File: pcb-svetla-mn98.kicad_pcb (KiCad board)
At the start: 2 copper layers, 32 x 35.6 mm, 7 parts, among them J1 TURN PAIRS, J14 P6DC INPUT, J2 MAIN LIGHTS, J3 AUX LIGHTS

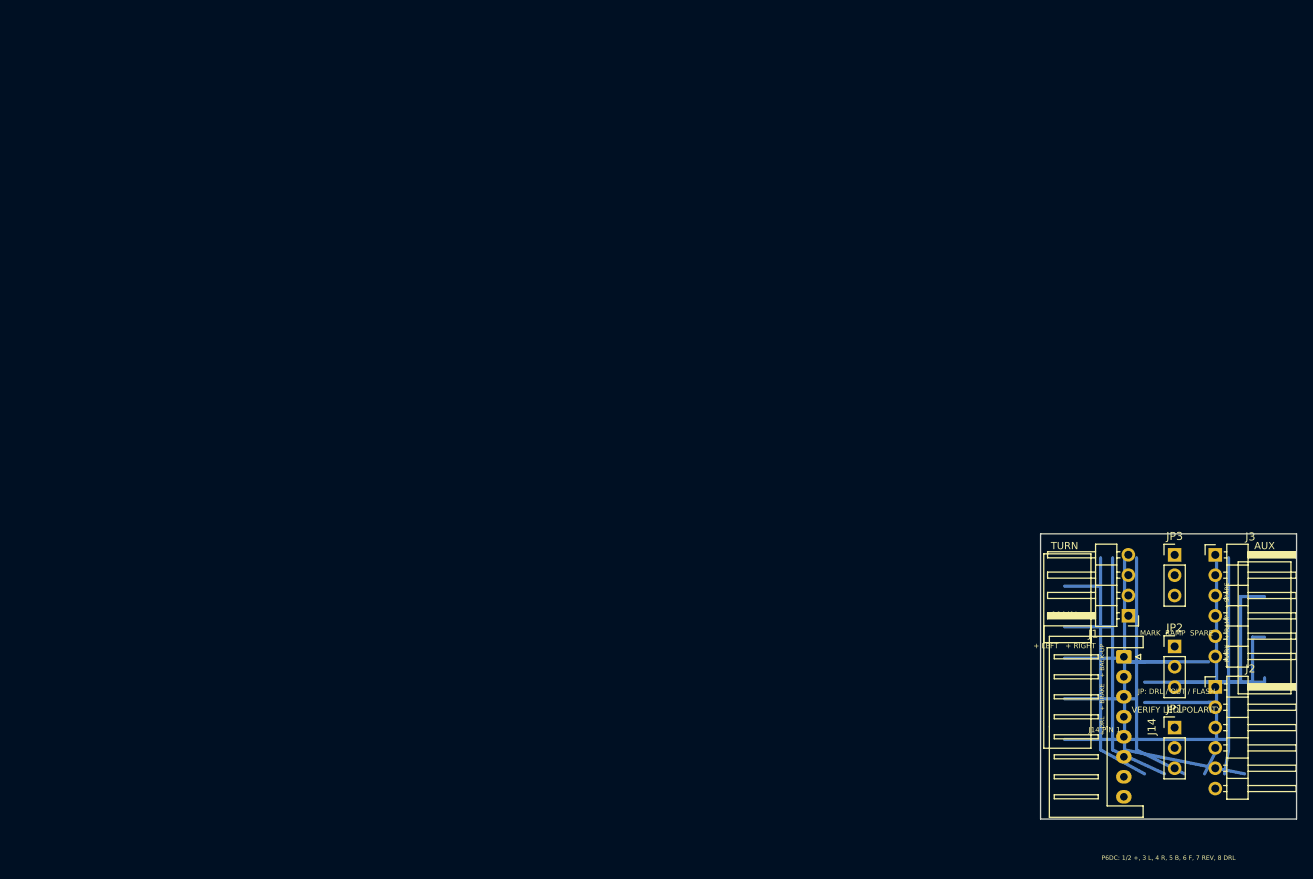
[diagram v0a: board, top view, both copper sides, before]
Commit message: Revise body distributor placement
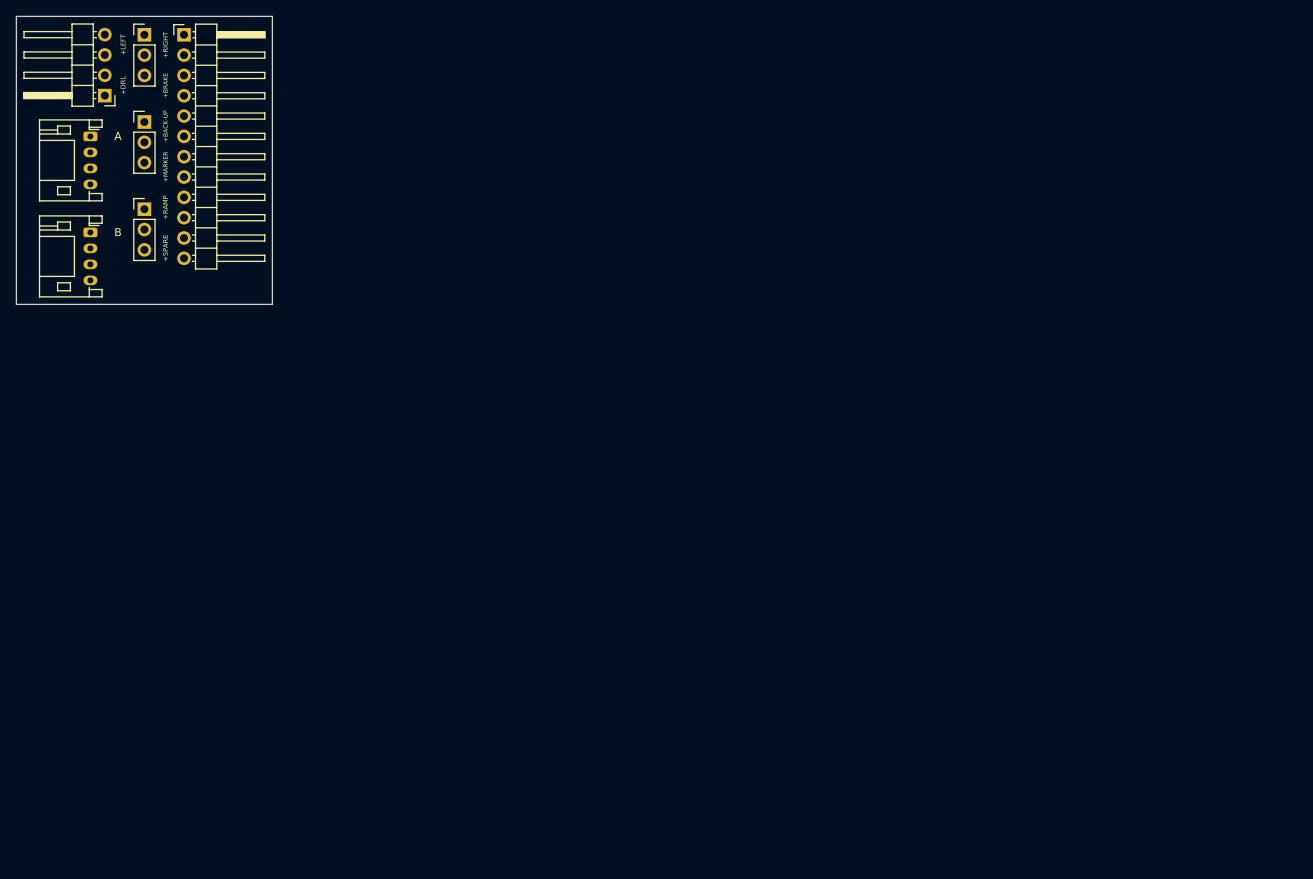
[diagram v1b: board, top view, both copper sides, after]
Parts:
- removed J3: AUX LIGHTS, PinHeader_1x06_P2.54mm_Horizontal
- added J15: BODY LINK B, JST_PH_S4B-PH-K_1x04_P2.00mm_Horizontal, F.Cu at (9.25, 27.0)
- J1: value TURN PAIRS -> LEFT LIGHT PORTS
- J14: value P6DC INPUT -> BODY LINK A; footprint JST_XH_S8B-XH-A_1x08_P2.50mm_Horizontal -> JST_PH_S4B-PH-K_1x04_P2.00mm_Horizontal
- J2: value MAIN LIGHTS -> RIGHT LIGHT PORTS; footprint PinHeader_1x06_P2.54mm_Horizontal -> PinHeader_1x12_P2.54mm_Horizontal
- moved JP1 155.2 mm to (16.0, 2.30)
- moved J2 152.5 mm to (20.9, 2.30)
- moved J14 144.6 mm to (9.25, 15.0)
- moved JP2 144.5 mm to (16.0, 13.2)
- moved J1 143.5 mm to (11.1, 9.90)
- moved JP3 135.8 mm to (16.0, 24.1)
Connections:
- J1 pad 1: RIGHT -> DRL
- J14 pad 2: COMMON+ -> LEFT
- J14 pad 3: LEFT -> RIGHT
- J14 pad 4: RIGHT -> BRAKE
- J2 pad 1: BACK-UP -> COMMON+
- J2 pad 2: COMMON+ -> RIGHT
- J2 pad 3: BRAKE -> COMMON+
- J2 pad 4: COMMON+ -> BRAKE
- J2 pad 5: DRL -> COMMON+
- J2 pad 6: COMMON+ -> BACK-UP
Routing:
- net DRL: track 66.3 -> 0.00 mm
- net BACK-UP: track 47.5 -> 0.00 mm
- net FLASH: track 42.4 -> 0.00 mm
- net BRAKE: track 39.7 -> 0.00 mm
- net RIGHT: track 37.2 -> 0.00 mm
- net LEFT: track 34.8 -> 0.00 mm
- net MARKER: track 25.7 -> 0.00 mm
- net RAMP: track 16.6 -> 0.00 mm
- net SPARE: track 7.54 -> 0.00 mm
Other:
- board size 32 x 35.6 mm -> 32 x 36 mm
- board text added: "+BACK-UP"
- board text added: "+BRAKE"
- board text added: "+DRL"
- board text added: "+LEFT"
- board text added: "+MARKER"
- board text added: "+RAMP"
- board text added: "+RIGHT"
- board text added: "+SPARE"
- board text added: "A"
- board text added: "B"
- board text removed: "+ DRL + BRAKE + BACK-UP"
- board text removed: "+ LEFT + RIGHT"
- board text removed: "+ MARK + RAMP + SPARE"
- board text removed: "AUX"
- board text removed: "J14 PIN 1"
- board text removed: "JP: DRL / OUT / FLASH"
- board text removed: "MAIN"
- board text removed: "MARK RAMP SPARE"
- board text removed: "P6DC: 1/2 +, 3 L, 4 R, 5 B, 6 F, 7 REV, 8 DRL"
- board text removed: "TURN"
- board text removed: "VERIFY LED POLARITY"
